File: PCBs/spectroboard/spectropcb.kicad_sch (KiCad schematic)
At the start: 14 parts, among them J1 Conn_02x07_Odd_Even, J2 Conn_02x08_Odd_Even, J3 Conn_02x08_Odd_Even, J4 Conn_01x02_Pin, J6 SM04B-GHS-TB, Q1 2SA1015, U1 TCD1304DG, U2 SN74HC04N

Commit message: updated pcb
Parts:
- J4: footprint Connector_JST:JST_PH_B2B-PH-K_1x02_P2.00mm_Vertical -> Connector_JST:JST_GH_SM02B-GHS-TB_1x02-1MP_P1.25mm_Horizontal
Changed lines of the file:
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@@
 	(generator_version "9.0")
 	(paper "A4")
-	(text_box "Yep, Output of the CCD goes into an ADC input on the STM32"
-		(exclude_from_sim no)
-		(at 41.91 139.7 0)
-		(size 19.05 13.97)
-		(margins 0.9525 0.9525 0.9525 0.9525)
-		(stroke
-			(width 0)
-			(type solid)
-		)
-		(fill
-			(type none)
-		)
-		(effects
-			(font
-				(size 1.27 1.27)
-			)
-			(justify left top)
-		)
-	)
-	(text_box "PWM Signal (Master Clock 2MHz)"
-		(exclude_from_sim no)
-		(at 35.56 80.01 0)
-		(size 16.51 7.62)
-		(margins 0.9525 0.9525 0.9525 0.9525)
-		(stroke
-			(width 0)
-			(type solid)
-		)
-		(fill
-			(type none)
-		)
-		(effects
-			(font
-				(size 1.27 1.27)
-			)
-			(justify left top)
-		)
-	)
-	(text_box "PWM Clock Signal (Different Frequency)"
-		(exclude_from_sim no)
-		(at 69.85 92.71 0)
-		(size 17.78 8.89)
-		(margins 0.9525 0.9525 0.9525 0.9525)
-		(stroke
-			(width 0)
-			(type solid)
-		)
-		(fill
-			(type none)
-		)
-		(effects
-			(font
-				(size 1.27 1.27)
-			)
-			(justify left top)
-		)
-	)
-	(text_box "PWM Shifted Clock Frequency (Either this is for or from the SH or ICG)"
-		(exclude_from_sim no)
-		(at 35.56 113.03 0)
-		(size 17.78 15.24)
-		(margins 0.9525 0.9525 0.9525 0.9525)
-		(stroke
-			(width 0)
-			(type solid)
-		)
-		(fill
-			(type none)
-		)
-		(effects
-			(font
-				(size 1.27 1.27)
-			)
-			(justify left top)
-		)
-	)
 	(junction
 		(at 147.32 36.83)
@@
 			)
 		)
-		(property "Footprint" "Connector_JST:JST_PH_B2B-PH-K_1x02_P2.00mm_Vertical"
+		(property "Footprint" "Connector_JST:JST_GH_SM02B-GHS-TB_1x02-1MP_P1.25mm_Horizontal"
 			(at 233.68 26.67 0)
 			(effects

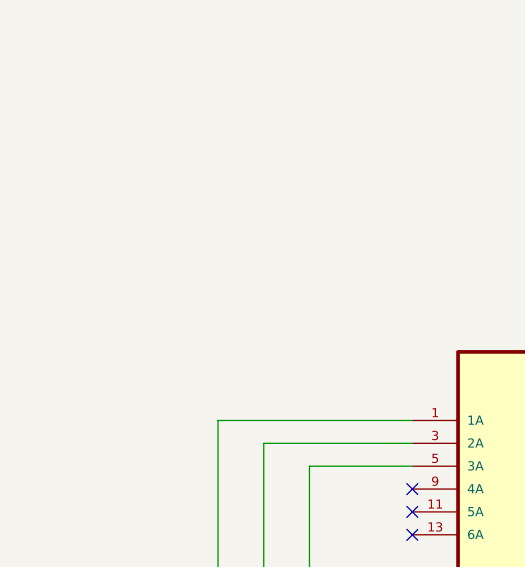
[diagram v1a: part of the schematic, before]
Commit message: mounting holes
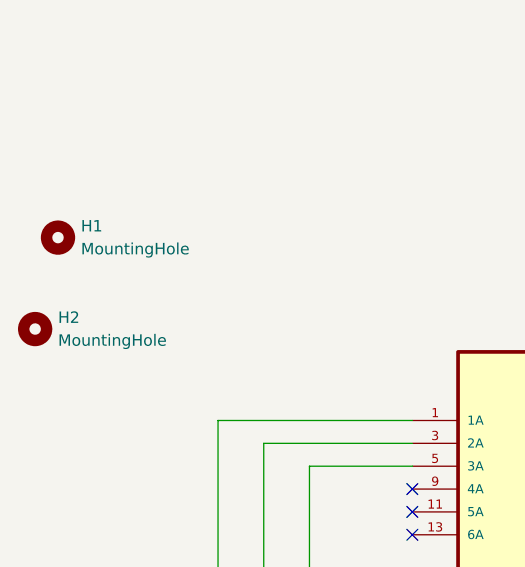
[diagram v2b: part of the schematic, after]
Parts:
- added H1, H2: MountingHole, MountingHole:MountingHole_3.2mm_M3, symbol Mechanical:MountingHole
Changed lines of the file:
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@@
+	)
+	(symbol
+		(lib_id "Mechanical:MountingHole")
+		(at 36.83 30.48 0)
+		(unit 1)
+		(exclude_from_sim no)
+		(in_bom no)
+		(on_board yes)
+		(dnp no)
+		(fields_autoplaced yes)
+		(property "Reference" "H1"
+			(at 39.37 29.2099 0)
+			(effects
+				(font
+					(size 1.27 1.27)
+				)
+				(justify left)
+			)
+		)
+		(property "Value" "MountingHole"
+			(at 39.37 31.7499 0)
+			(effects
+				(font
+					(size 1.27 1.27)
+				)
+				(justify left)
+			)
+		)
+		(property "Footprint" "MountingHole:MountingHole_3.2mm_M3"
+			(at 36.83 30.48 0)
+			(effects
+				(font
+					(size 1.27 1.27)
+				)
+				(hide yes)
+			)
+		)
+		(property "Datasheet" "~"
+			(at 36.83 30.48 0)
+			(effects
+				(font
+					(size 1.27 1.27)
+				)
+				(hide yes)
+			)
+		)
+		(property "Description" "Mounting Hole without connection"
+			(at 36.83 30.48 0)
+			(effects
+				(font
+					(size 1.27 1.27)
+				)
+				(hide yes)
+			)
+		)
+		(instances
+			(project ""
+				(path "/705004fe-9694-4831-a243-8c72357320a8"
+					(reference "H1")
+					(unit 1)
+				)
+			)
+		)
 	)
 	(symbol
@@
 					(unit 1)
 				)
+			)
+		)
+	)
+	(symbol
+		(lib_id "Mechanical:MountingHole")
+		(at 34.29 40.64 0)
+		(unit 1)
+		(exclude_from_sim no)
+		(in_bom no)
+		(on_board yes)
+		(dnp no)
+		(fields_autoplaced yes)
+		(property "Reference" "H2"
+			(at 36.83 39.3699 0)
+			(effects
+				(font
+					(size 1.27 1.27)
+				)
+				(justify left)
+			)
+		)
+		(property "Value" "MountingHole"
+			(at 36.83 41.9099 0)
+			(effects
+				(font
+					(size 1.27 1.27)
+				)
+				(justify left)
+			)
+		)
+		(property "Footprint" "MountingHole:MountingHole_3.2mm_M3"
+			(at 34.29 40.64 0)
+			(effects
+				(font
+					(size 1.27 1.27)
+				)
+				(hide yes)
+			)
+		)
+		(property "Datasheet" "~"
+			(at 34.29 40.64 0)
+			(effects
+				(font
+					(size 1.27 1.27)
+				)
+				(hide yes)
+			)
+		)
+		(property "Description" "Mounting Hole without connection"
+			(at 34.29 40.64 0)
+			(effects
+				(font
+					(size 1.27 1.27)
+				)
+				(hide yes)
+			)
+		)
+		(instances
+			(project "spectropcb"
+				(path "/705004fe-9694-4831-a243-8c72357320a8"
+					(reference "H2")
+					(unit 1)
+				)

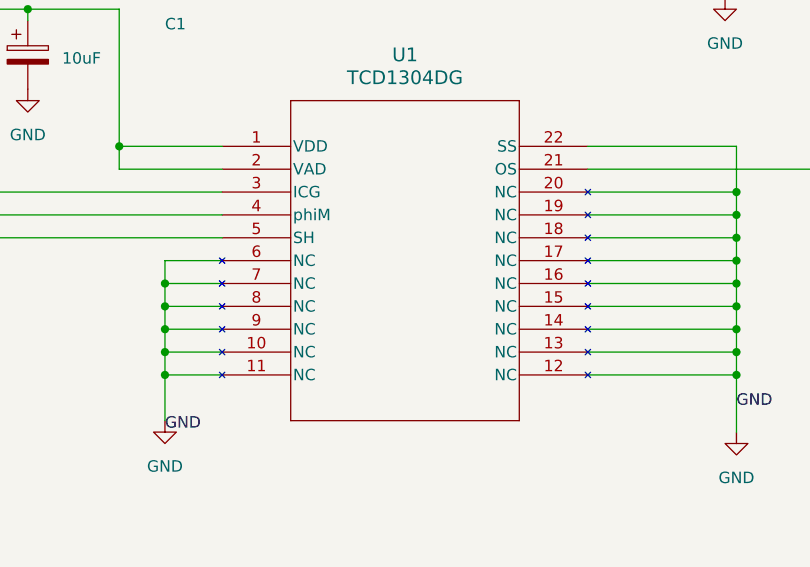
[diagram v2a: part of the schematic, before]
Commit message: grounded ccd
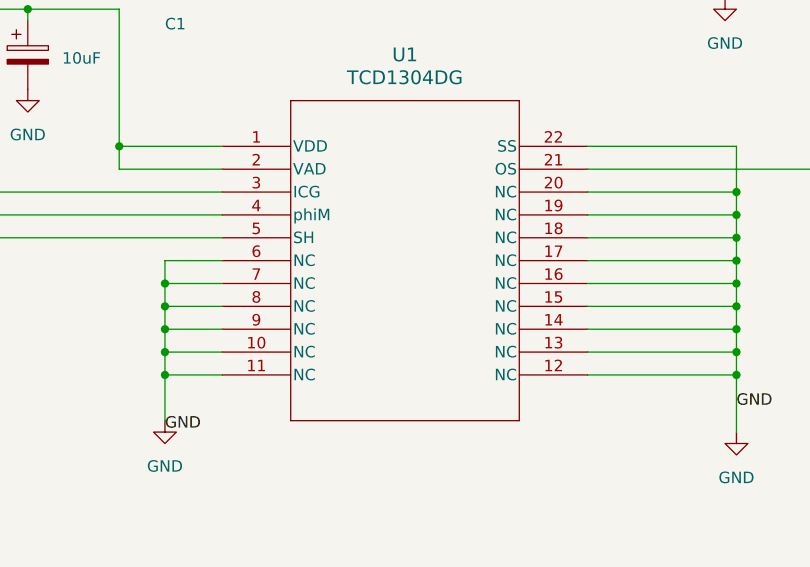
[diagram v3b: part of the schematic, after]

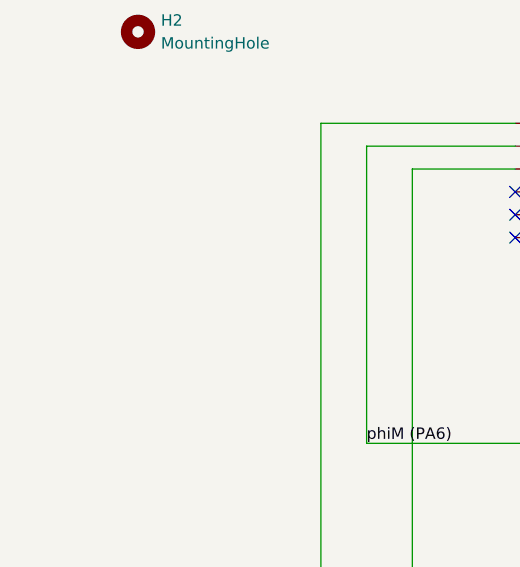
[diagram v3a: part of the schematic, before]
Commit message: 4 mounts
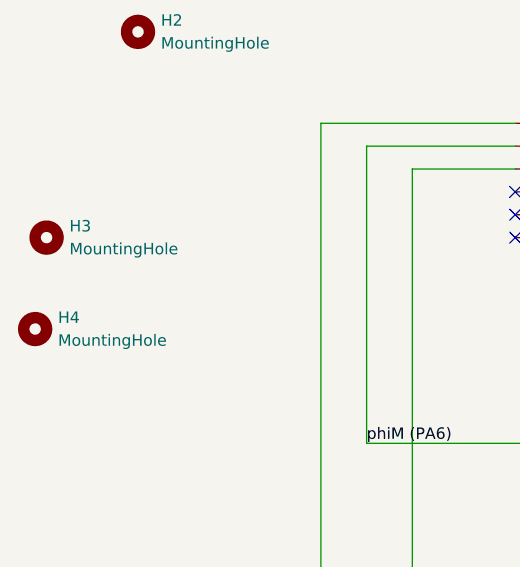
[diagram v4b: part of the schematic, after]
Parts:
- added H3, H4: MountingHole, MountingHole:MountingHole_3.2mm_M3, symbol Mechanical:MountingHole
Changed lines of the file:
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@@
+	)
+	(symbol
+		(lib_id "Mechanical:MountingHole")
+		(at 22.86 73.66 0)
+		(unit 1)
+		(exclude_from_sim no)
+		(in_bom no)
+		(on_board yes)
+		(dnp no)
+		(fields_autoplaced yes)
+		(property "Reference" "H4"
+			(at 25.4 72.3899 0)
+			(effects
+				(font
+					(size 1.27 1.27)
+				)
+				(justify left)
+			)
+		)
+		(property "Value" "MountingHole"
+			(at 25.4 74.9299 0)
+			(effects
+				(font
+					(size 1.27 1.27)
+				)
+				(justify left)
+			)
+		)
+		(property "Footprint" "MountingHole:MountingHole_3.2mm_M3"
+			(at 22.86 73.66 0)
+			(effects
+				(font
+					(size 1.27 1.27)
+				)
+				(hide yes)
+			)
+		)
+		(property "Datasheet" "~"
+			(at 22.86 73.66 0)
+			(effects
+				(font
+					(size 1.27 1.27)
+				)
+				(hide yes)
+			)
+		)
+		(property "Description" "Mounting Hole without connection"
+			(at 22.86 73.66 0)
+			(effects
+				(font
+					(size 1.27 1.27)
+				)
+				(hide yes)
+			)
+		)
+		(instances
+			(project "spectropcb"
+				(path "/705004fe-9694-4831-a243-8c72357320a8"
+					(reference "H4")
+					(unit 1)
+				)
+			)
+		)
 	)
 	(symbol
@@
 					(unit 1)
 				)
+			)
+		)
+	)
+	(symbol
+		(lib_id "Mechanical:MountingHole")
+		(at 24.13 63.5 0)
+		(unit 1)
+		(exclude_from_sim no)
+		(in_bom no)
+		(on_board yes)
+		(dnp no)
+		(fields_autoplaced yes)
+		(property "Reference" "H3"
+			(at 26.67 62.2299 0)
+			(effects
+				(font
+					(size 1.27 1.27)
+				)
+				(justify left)
+			)
+		)
+		(property "Value" "MountingHole"
+			(at 26.67 64.7699 0)
+			(effects
+				(font
+					(size 1.27 1.27)
+				)
+				(justify left)
+			)
+		)
+		(property "Footprint" "MountingHole:MountingHole_3.2mm_M3"
+			(at 24.13 63.5 0)
+			(effects
+				(font
+					(size 1.27 1.27)
+				)
+				(hide yes)
+			)
+		)
+		(property "Datasheet" "~"
+			(at 24.13 63.5 0)
+			(effects
+				(font
+					(size 1.27 1.27)
+				)
+				(hide yes)
+			)
+		)
+		(property "Description" "Mounting Hole without connection"
+			(at 24.13 63.5 0)
+			(effects
+				(font
+					(size 1.27 1.27)
+				)
+				(hide yes)
+			)
+		)
+		(instances
+			(project "spectropcb"
+				(path "/705004fe-9694-4831-a243-8c72357320a8"
+					(reference "H3")
+					(unit 1)
+				)
